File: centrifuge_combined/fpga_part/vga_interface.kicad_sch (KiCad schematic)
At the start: 19 parts, among them J3 Conn_01x15, Q3 BSN20, Q4 BSN20, U13 PESD4USB5B-TTS, U9 LSF0102

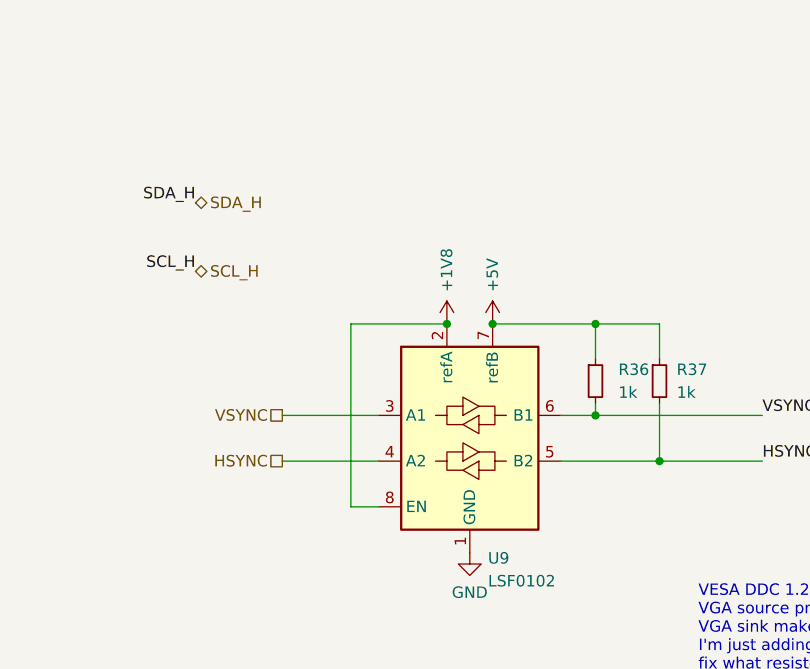
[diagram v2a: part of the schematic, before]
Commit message: fix elprint complaints, except intranet clearance, also widen some traces
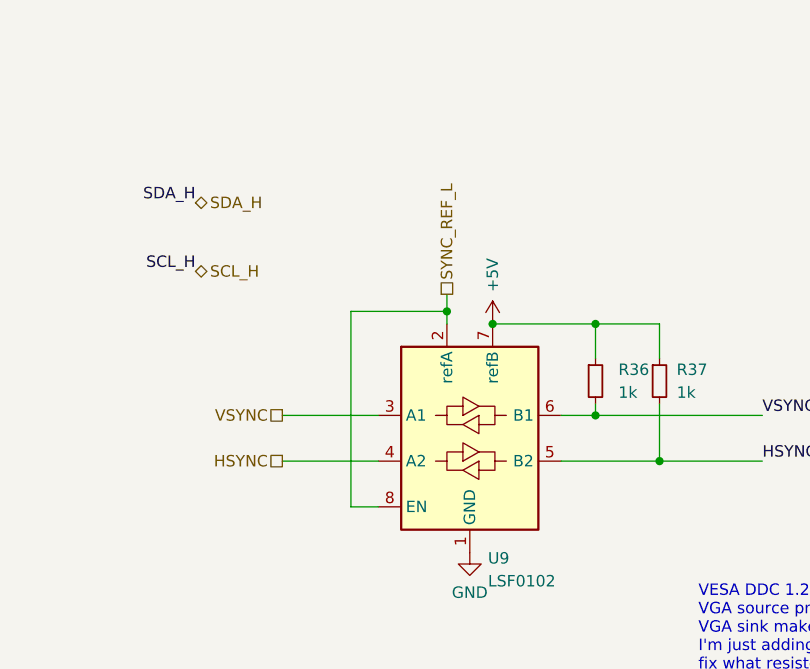
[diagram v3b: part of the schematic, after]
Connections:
- net +1V8_FPGA renamed SYNC_REF_L
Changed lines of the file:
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@@
   (junction (at 238.125 59.69) (diameter 0) (color 0 0 0 0)
   )
-  (junction (at 146.05 117.602) (diameter 0) (color 0 0 0 0)
-  )
   (junction (at 66.04 45.72) (diameter 0) (color 0 0 0 0)
   )
@@
   )
   (junction (at 66.04 73.025) (diameter 0) (color 0 0 0 0)
+  )
+  (junction (at 146.05 116.205) (diameter 0) (color 0 0 0 0)
   )
   (junction (at 99.695 73.025) (diameter 0) (color 0 0 0 0)
@@
     (stroke (width 0) (type default) (color 0 0 0 0))
   )
-  (wire (pts (xy 135.382 137.922) (xy 135.382 117.602))
+  (wire (pts (xy 146.05 114.3) (xy 146.05 116.205))
+    (stroke (width 0) (type default) (color 0 0 0 0))
+  )
+  (wire (pts (xy 135.382 137.922) (xy 135.382 116.205))
     (stroke (width 0) (type default) (color 0 0 0 0))
   )
@@
     (stroke (width 0) (type default) (color 0 0 0 0))
   )
+  (wire (pts (xy 146.05 116.205) (xy 146.05 117.602))
+    (stroke (width 0) (type default) (color 0 0 0 0))
+  )
   (wire (pts (xy 225.425 67.31) (xy 238.125 67.31))
     (stroke (width 0) (type default) (color 0 0 0 0))
@@
     (stroke (width 0) (type default) (color 0 0 0 0))
   )
-  (wire (pts (xy 135.382 117.602) (xy 146.05 117.602))
+  (wire (pts (xy 135.382 116.205) (xy 146.05 116.205))
     (stroke (width 0) (type default) (color 0 0 0 0))
   )
@@
   (hierarchical_label "VSYNC" (shape passive) (at 127.762 127.762 180)
     (effects (font (size 1.27 1.27)) (justify right))
+  )
+  (hierarchical_label "SYNC_REF_L" (shape passive) (at 146.05 114.3 90)
+    (effects (font (size 1.27 1.27)) (justify left))
   )
   (hierarchical_label "SDA_H" (shape tri_state) (at 118.11 104.14 0)
@@
       (effects (font (size 1.27 1.27)) hide)
     )
-    (pin "1")
-  )
-  (symbol (lib_id "centrifuge_symbols:+1V8_FPGA") (at 146.05 117.602 0) (unit 1)
-    (in_bom yes) (on_board yes) (fields_autoplaced)
-    (property "Reference" "#PWR0177" (id 0) (at 146.05 121.412 0)
-      (effects (font (size 1.27 1.27)) hide)
-    )
-    (property "Value" "+1V8" (id 1) (at 146.05 114.046 90)
-      (effects (font (size 1.27 1.27)) (justify left))
-    )
-    (property "Footprint" "" (id 2) (at 146.05 117.602 0)
-      (effects (font (size 1.27 1.27)) hide)
-    )
-    (property "Datasheet" "" (id 3) (at 146.05 117.602 0)
-      (effects (font (size 1.27 1.27)) hide)
-    )

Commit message: more checks, also make silkscreen text for connectors
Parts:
- U9: Purchase (none) -> BOUGHT https://www.digikey.no/no/products/detail/nexperia-u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
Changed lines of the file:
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@@
+      (effects (font (size 1.27 1.27)) hide)
+    )
+    (property "Purchase" "BOUGHT https://www.digikey.no/no/products/detail/nexperia-usa-inc/LSF0102DCH/13574967" (id 4) (at 148.59 130.302 0)
       (effects (font (size 1.27 1.27)) hide)
     )

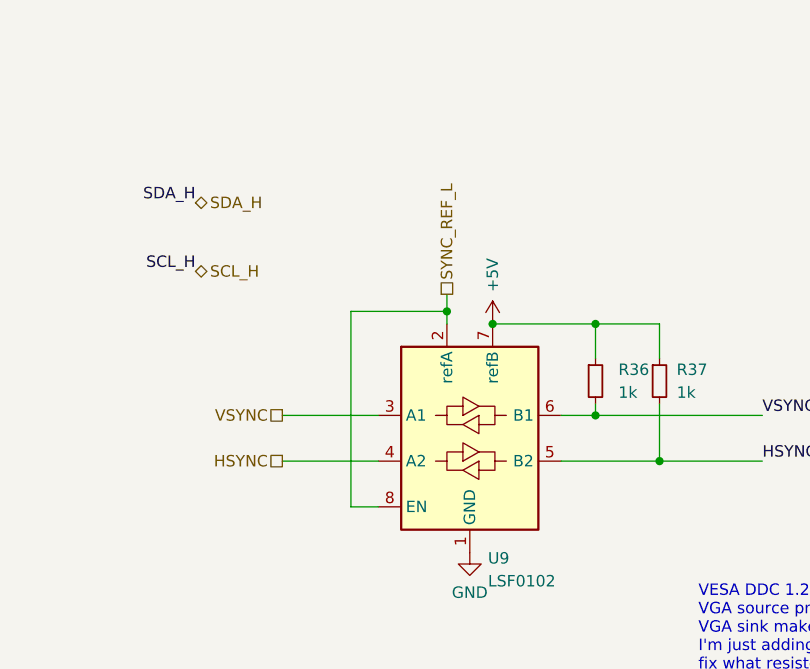
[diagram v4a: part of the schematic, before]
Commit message: Fixed Elprint complaints and JTAG VREF problems+config flash CS
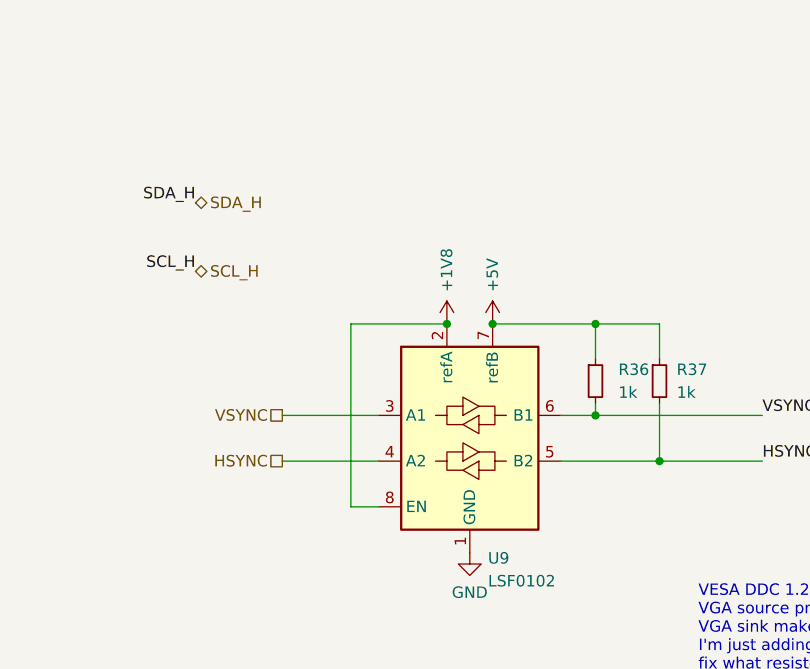
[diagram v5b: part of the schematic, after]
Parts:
- U9: Purchase BOUGHT https://www.digikey.no/no/products/detail/nexperia-u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 -> (none)
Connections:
- net SYNC_REF_L renamed +1V8_FPGA
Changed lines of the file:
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@@
   (title_block
     (title "VGA Centrifuge")
-    (date "2022-10-03")
-    (rev "R3")
+    (date "2022-10-05")
+    (rev "R4")
     (comment 1 "Author: Paolo Celati")
     (comment 2 "VGA connector interfacing")
@@
   (junction (at 238.125 59.69) (diameter 0) (color 0 0 0 0)
   )
+  (junction (at 146.05 117.602) (diameter 0) (color 0 0 0 0)
+  )
   (junction (at 66.04 45.72) (diameter 0) (color 0 0 0 0)
   )
@@
   )
   (junction (at 66.04 73.025) (diameter 0) (color 0 0 0 0)
-  )
-  (junction (at 146.05 116.205) (diameter 0) (color 0 0 0 0)
   )
   (junction (at 99.695 73.025) (diameter 0) (color 0 0 0 0)
@@
     (stroke (width 0) (type default) (color 0 0 0 0))
   )
-  (wire (pts (xy 146.05 114.3) (xy 146.05 116.205))
-    (stroke (width 0) (type default) (color 0 0 0 0))
-  )
-  (wire (pts (xy 135.382 137.922) (xy 135.382 116.205))
+  (wire (pts (xy 135.382 137.922) (xy 135.382 117.602))
     (stroke (width 0) (type default) (color 0 0 0 0))
   )
@@
     (stroke (width 0) (type default) (color 0 0 0 0))
   )
-  (wire (pts (xy 146.05 116.205) (xy 146.05 117.602))
-    (stroke (width 0) (type default) (color 0 0 0 0))
-  )
   (wire (pts (xy 225.425 67.31) (xy 238.125 67.31))
     (stroke (width 0) (type default) (color 0 0 0 0))
@@
     (stroke (width 0) (type default) (color 0 0 0 0))
   )
-  (wire (pts (xy 135.382 116.205) (xy 146.05 116.205))
+  (wire (pts (xy 135.382 117.602) (xy 146.05 117.602))
     (stroke (width 0) (type default) (color 0 0 0 0))
   )
@@
   (hierarchical_label "VSYNC" (shape passive) (at 127.762 127.762 180)
     (effects (font (size 1.27 1.27)) (justify right))
-  )
-  (hierarchical_label "SYNC_REF_L" (shape passive) (at 146.05 114.3 90)
-    (effects (font (size 1.27 1.27)) (justify left))
   )
   (hierarchical_label "SDA_H" (shape tri_state) (at 118.11 104.14 0)
@@
     )
     (property "Datasheet" "" (id 3) (at 99.695 34.29 0)
+      (effects (font (size 1.27 1.27)) hide)
+    )
+    (pin "1")
+  )
+  (symbol (lib_id "centrifuge_symbols:+1V8_FPGA") (at 146.05 117.602 0) (unit 1)
+    (in_bom yes) (on_board yes) (fields_autoplaced)
+    (property "Reference" "#PWR0177" (id 0) (at 146.05 121.412 0)
+      (effects (font (size 1.27 1.27)) hide)
+    )
+    (property "Value" "+1V8" (id 1) (at 146.05 114.046 90)
+      (effects (font (size 1.27 1.27)) (justify left))
+    )
+    (property "Footprint" "" (id 2) (at 146.05 117.602 0)
+      (effects (font (size 1.27 1.27)) hide)
+    )
+    (property "Datasheet" "" (id 3) (at 146.05 117.602 0)
       (effects (font (size 1.27 1.27)) hide)
     )
@@
       (effects (font (size 1.27 1.27)) hide)
     )
-    (property "Purchase" "BOUGHT https://www.digikey.no/no/products/detail/nexperia-usa-inc/LSF0102DCH/13574967" (id 4) (at 148.59 130.302 0)
-      (effects (font (size 1.27 1.27)) hide)
-    )
